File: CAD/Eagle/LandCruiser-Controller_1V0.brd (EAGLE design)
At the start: 99 x 67.7 mm, 21 parts, among them U101 MEGA8-P, X301 I2C

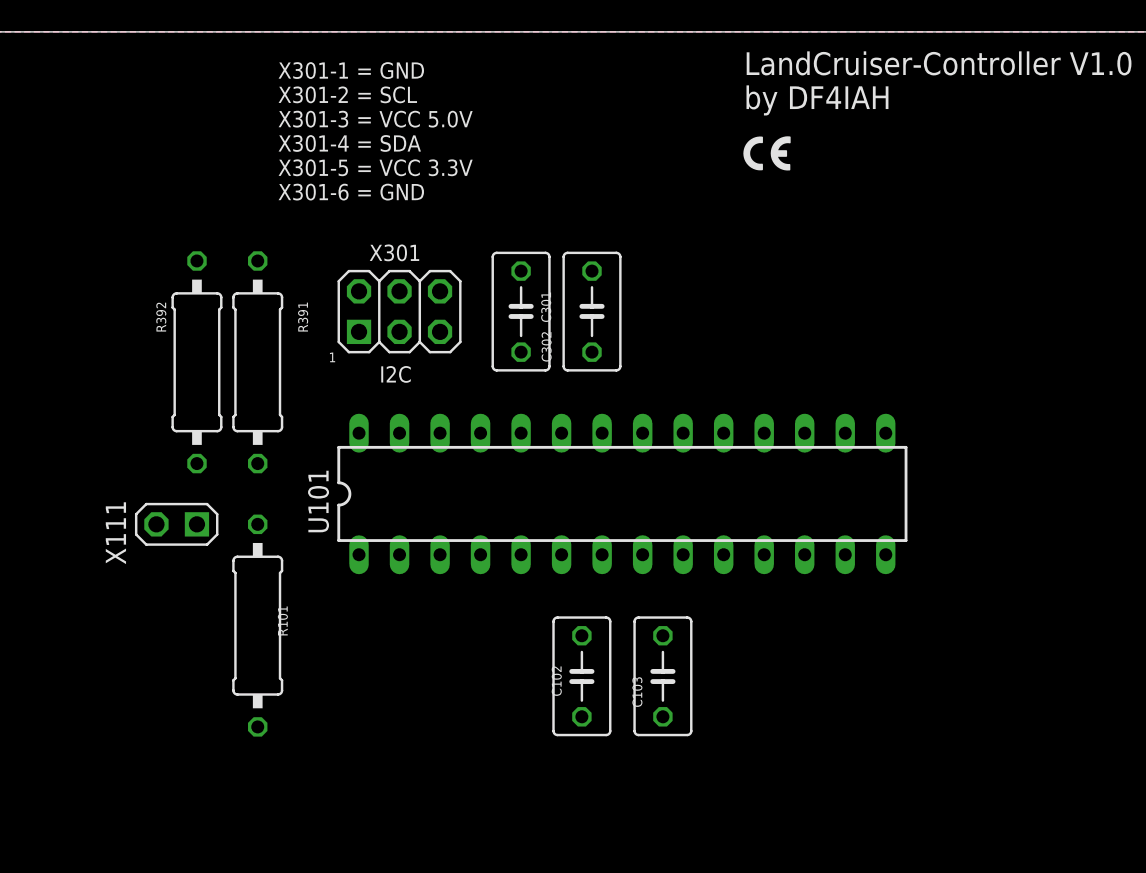
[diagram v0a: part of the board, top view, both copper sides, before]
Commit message: HW - pull-down resistors added to the ATmega output lines
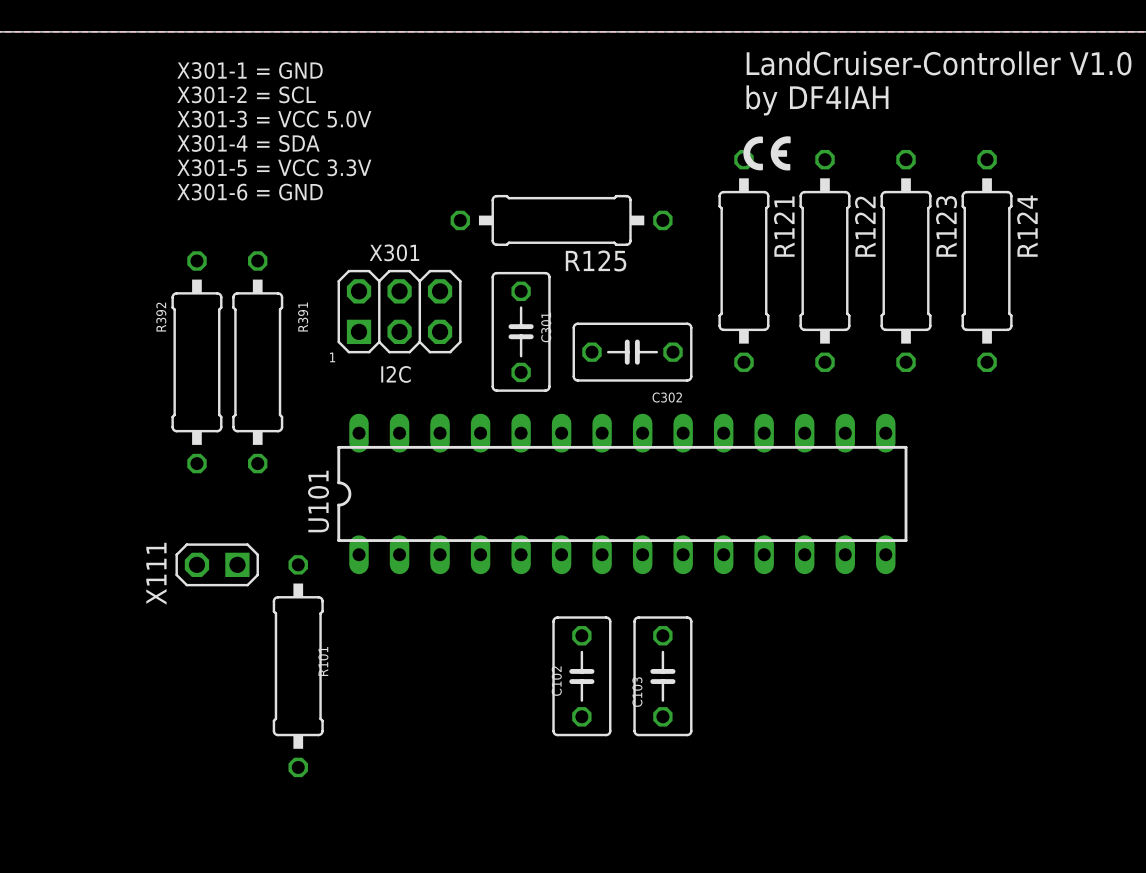
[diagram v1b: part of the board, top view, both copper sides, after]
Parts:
- added R121, R122, R123, R124, R125: 33kR, rcl:0309/12
- moved C302 3.59 mm to (50.2, 47.6), turned to 180 degrees
- moved R101 3.59 mm to (29.2, 27.9)
- moved X111 3.59 mm to (25.4, 34.3)
- moved C301 1.27 mm to (43.2, 48.9)
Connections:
- net GND: now also R121.1, R122.1, R123.1, R124.1, R125.1
- net MP_KL: now also R125.2
- net MP_M1: now also R123.2
- net MP_M2: now also R124.2
- net MP_PV_G: now also R121.2
- net MP_PV_O: now also R122.2
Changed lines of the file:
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@@
 <dimension x1="0" y1="0" x2="0" y2="7.5" x3="-3.5" y3="3.75" textsize="0.6096" layer="47"/>
 <text x="31.115" y="46.99" size="0.6096" layer="21" ratio="20">1</text>
-<text x="27.94" y="57.15" size="1.016" layer="21">X301-1 = GND
+<text x="21.59" y="57.15" size="1.016" layer="21">X301-1 = GND
 X301-2 = SCL
 X301-3 = VCC 5.0V
@@
 <attribute name="VALUE" x="23.495" y="45.72" size="0.6096" layer="27" rot="R90"/>
 </element>
-<element name="C302" library="rcl" package="C050-035X075" value="100nF" x="47.625" y="50.165" smashed="yes" rot="R90">
-<attribute name="NAME" x="45.085" y="46.99" size="0.6096" layer="25" rot="R90"/>
-<attribute name="VALUE" x="48.26" y="48.895" size="0.6096" layer="27" rot="R90"/>
-</element>
-<element name="C301" library="rcl" package="C050-035X075" value="100nF" x="43.18" y="50.165" smashed="yes" rot="R90">
-<attribute name="NAME" x="44.45" y="51.435" size="0.6096" layer="25" rot="R270"/>
-<attribute name="VALUE" x="42.545" y="51.435" size="0.6096" layer="27" rot="R270"/>
+<element name="C302" library="rcl" package="C050-035X075" value="100nF" x="50.165" y="47.625" smashed="yes" rot="R180">
+<attribute name="NAME" x="53.34" y="45.085" size="0.6096" layer="25" rot="R180"/>
+<attribute name="VALUE" x="51.435" y="48.26" size="0.6096" layer="27" rot="R180"/>
+</element>
+<element name="C301" library="rcl" package="C050-035X075" value="100nF" x="43.18" y="48.895" smashed="yes" rot="R90">
+<attribute name="NAME" x="44.45" y="50.165" size="0.6096" layer="25" rot="R270"/>
+<attribute name="VALUE" x="42.545" y="50.165" size="0.6096" layer="27" rot="R270"/>
 </element>
 <element name="C102" library="rcl" package="C050-035X075" value="100nF" x="46.99" y="27.305" smashed="yes" rot="R270">
@@
 <attribute name="VALUE" x="52.705" y="26.035" size="0.6096" layer="27" rot="R90"/>
 </element>
-<element name="R101" library="rcl" package="0309/12" value="12kR" x="26.67" y="30.48" smashed="yes" rot="R90">
-<attribute name="NAME" x="27.94" y="31.75" size="0.6096" layer="25" rot="R270"/>
-<attribute name="VALUE" x="26.035" y="31.115" size="0.6096" layer="27" rot="R270"/>
+<element name="R101" library="rcl" package="0309/12" value="12kR" x="29.21" y="27.94" smashed="yes" rot="R90">
+<attribute name="NAME" x="30.48" y="29.21" size="0.6096" layer="25" rot="R270"/>
+<attribute name="VALUE" x="28.575" y="28.575" size="0.6096" layer="27" rot="R270"/>
 </element>
 <element name="U101" library="df4iah_processors" package="DIL28-3" value="MEGA8-P" x="49.53" y="38.735"/>
@@
 <element name="FM503" library="df4iah_fiducial" package="FIDUCIAL_MARK_1MM" value="FIDUCIAL_MARK_1MM" x="95.25" y="54.61"/>
 <element name="FM504" library="df4iah_fiducial" package="FIDUCIAL_MARK_1MM" value="FIDUCIAL_MARK_1MM" x="95.25" y="11.43"/>
-<element name="X111" library="df4iah_connector" package="1X02" value="" x="22.86" y="36.83" rot="R90"/>
+<element name="X111" library="df4iah_connector" package="1X02" value="" x="25.4" y="34.29" rot="R90"/>
+<element name="R121" library="rcl" package="0309/12" value="33kR" x="57.15" y="53.34" rot="R270"/>
+<element name="R123" library="rcl" package="0309/12" value="33kR" x="67.31" y="53.34" rot="R270"/>
+<element name="R125" library="rcl" package="0309/12" value="33kR" x="45.72" y="55.88" rot="R180"/>
+<element name="R122" library="rcl" package="0309/12" value="33kR" x="62.23" y="53.34" rot="R270"/>
+<element name="R124" library="rcl" package="0309/12" value="33kR" x="72.39" y="53.34" rot="R270"/>
 </elements>
 <signals>
@@
 <vertex x="99.06" y="0"/>
 </polygon>
-<contactref element="C102" pad="2"/>
 <contactref element="C101" pad="2"/>
 <contactref element="U101" pad="8"/>
@@
 <contactref element="H504" pad="B2,8"/>
 <contactref element="X111" pad="2"/>
+<contactref element="R125" pad="1"/>
+<contactref element="R122" pad="1"/>
+<contactref element="R124" pad="1"/>
+<contactref element="R121" pad="1"/>
+<contactref element="R123" pad="1"/>
+<contactref element="C102" pad="2"/>
+<wire x1="72.39" y1="59.69" x2="93.77" y2="62.5" width="0" layer="19" extent="1-1"/>
+<wire x1="67.31" y1="59.69" x2="72.39" y2="59.69" width="0" layer="19" extent="1-1"/>
+<wire x1="62.23" y1="59.69" x2="67.31" y2="59.69" width="0" layer="19" extent="1-1"/>
+<wire x1="57.15" y1="59.69" x2="62.23" y2="59.69" width="0" layer="19" extent="1-1"/>
+<wire x1="52.07" y1="55.88" x2="57.15" y2="59.69" width="0" layer="19" extent="1-1"/>
+<wire x1="47.625" y1="47.625" x2="52.07" y2="55.88" width="0" layer="19" extent="1-1"/>
+<wire x1="48.26" y1="42.545" x2="47.625" y2="47.625" width="0" layer="19" extent="1-1"/>
+<wire x1="43.18" y1="51.435" x2="47.625" y2="47.625" width="0" layer="19" extent="1-1"/>
+<wire x1="38.1" y1="51.435" x2="43.18" y2="51.435" width="0" layer="19" extent="1-1"/>
+<wire x1="33.02" y1="48.895" x2="38.1" y2="51.435" width="0" layer="19" extent="1-1"/>
+<wire x1="50.8" y1="34.925" x2="48.26" y2="42.545" width="0" layer="19" extent="1-1"/>
+<wire x1="52.07" y1="29.845" x2="50.8" y2="34.925" width="0" layer="19" extent="1-1"/>
+<wire x1="46.99" y1="24.765" x2="52.07" y2="29.845" width="0" layer="19" extent="1-1"/>
+<wire x1="22.86" y1="34.29" x2="33.02" y2="48.895" width="0" layer="19" extent="1-1"/>
+<wire x1="4.96" y1="62.5" x2="33.02" y2="48.895" width="0" layer="19" extent="1-1"/>
 <wire x1="92.71" y1="29.972" x2="93.77" y2="62.5" width="0" layer="19" extent="1-1"/>
 <wire x1="93.77" y1="4.96" x2="92.71" y2="29.972" width="0" layer="19" extent="1-1"/>
-<wire x1="52.07" y1="29.845" x2="92.71" y2="29.972" width="0" layer="19" extent="1-1"/>
-<wire x1="50.8" y1="34.925" x2="52.07" y2="29.845" width="0" layer="19" extent="1-1"/>
-<wire x1="46.99" y1="24.765" x2="52.07" y2="29.845" width="0" layer="19" extent="1-1"/>
-<wire x1="48.26" y1="42.545" x2="50.8" y2="34.925" width="0" layer="19" extent="1-1"/>
-<wire x1="47.625" y1="52.705" x2="48.26" y2="42.545" width="0" layer="19" extent="1-1"/>
-<wire x1="43.18" y1="52.705" x2="47.625" y2="52.705" width="0" layer="19" extent="1-1"/>
-<wire x1="38.1" y1="51.435" x2="43.18" y2="52.705" width="0" layer="19" extent="1-1"/>
-<wire x1="33.02" y1="48.895" x2="38.1" y2="51.435" width="0" layer="19" extent="1-1"/>
-<wire x1="20.32" y1="36.83" x2="33.02" y2="48.895" width="0" layer="19" extent="1-1"/>
-<wire x1="4.96" y1="62.5" x2="20.32" y2="36.83" width="0" layer="19" extent="1-1"/>
-<wire x1="4.96" y1="4.96" x2="20.32" y2="36.83" width="0" layer="19" extent="1-1"/>
+<wire x1="4.96" y1="4.96" x2="22.86" y2="34.29" width="0" layer="19" extent="1-1"/>
 </signal>
 <signal name="+5V">
 <contactref element="X301" pad="3"/>
 <contactref element="C301" pad="1"/>
-<wire x1="35.56" y1="48.895" x2="43.18" y2="47.625" width="0" layer="19" extent="1-1"/>
+<wire x1="35.56" y1="48.895" x2="43.18" y2="46.355" width="0" layer="19" extent="1-1"/>
 </signal>
 <signal name="+3V3">
@@
 <contactref element="U101" pad="7"/>
 <wire x1="53.34" y1="42.545" x2="92.71" y2="44.958" width="0" layer="19" extent="1-1"/>
-<wire x1="47.625" y1="47.625" x2="53.34" y2="42.545" width="0" layer="19" extent="1-1"/>
+<wire x1="52.705" y1="47.625" x2="53.34" y2="42.545" width="0" layer="19" extent="1-1"/>
 <wire x1="48.26" y1="34.925" x2="53.34" y2="42.545" width="0" layer="19" extent="1-1"/>
 <wire x1="46.99" y1="29.845" x2="48.26" y2="34.925" width="0" layer="19" extent="1-1"/>
-<wire x1="38.1" y1="48.895" x2="47.625" y2="47.625" width="0" layer="19" extent="1-1"/>
+<wire x1="38.1" y1="48.895" x2="52.705" y2="47.625" width="0" layer="19" extent="1-1"/>
 <wire x1="26.67" y1="53.34" x2="38.1" y2="48.895" width="0" layer="19" extent="1-1"/>
 <wire x1="22.86" y1="53.34" x2="26.67" y2="53.34" width="0" layer="19" extent="1-1"/>
-<wire x1="26.67" y1="24.13" x2="46.99" y2="29.845" width="0" layer="19" extent="1-1"/>
+<wire x1="29.21" y1="21.59" x2="46.99" y2="29.845" width="0" layer="19" extent="1-1"/>
 </signal>
 <signal name="SCL">
@@
 <contactref element="R101" pad="2"/>
 <contactref element="X111" pad="1"/>
-<wire x1="26.67" y1="36.83" x2="33.02" y2="34.925" width="0" layer="19" extent="1-1"/>
-<wire x1="22.86" y1="36.83" x2="26.67" y2="36.83" width="0" layer="19" extent="1-1"/>
+<wire x1="29.21" y1="34.29" x2="33.02" y2="34.925" width="0" layer="19" extent="1-1"/>
+<wire x1="25.4" y1="34.29" x2="29.21" y2="34.29" width="0" layer="19" extent="1-1"/>
 </signal>
 <signal name="AREF">
@@
 <signal name="MP_M2">
 <contactref element="U101" pad="16"/>
+<contactref element="R124" pad="2"/>
+<wire x1="63.5" y1="42.545" x2="72.39" y2="46.99" width="0" layer="19" extent="1-1"/>
 </signal>
 <signal name="MP_M1">
 <contactref element="U101" pad="17"/>
+<contactref element="R123" pad="2"/>
+<wire x1="60.96" y1="42.545" x2="67.31" y2="46.99" width="0" layer="19" extent="1-1"/>
 </signal>
 <signal name="MP_PV_O">
 <contactref element="U101" pad="18"/>
+<contactref element="R122" pad="2"/>
+<wire x1="58.42" y1="42.545" x2="62.23" y2="46.99" width="0" layer="19" extent="1-1"/>
 </signal>
 <signal name="MP_PV_G">
 <contactref element="U101" pad="19"/>
+<contactref element="R121" pad="2"/>
+<wire x1="55.88" y1="42.545" x2="57.15" y2="46.99" width="0" layer="19" extent="1-1"/>
 </signal>
 <signal name="MP_KL">
 <contactref element="U101" pad="26"/>
+<contactref element="R125" pad="2"/>
+<wire x1="38.1" y1="42.545" x2="39.37" y2="55.88" width="0" layer="19" extent="1-1"/>
 </signal>
 </signals>

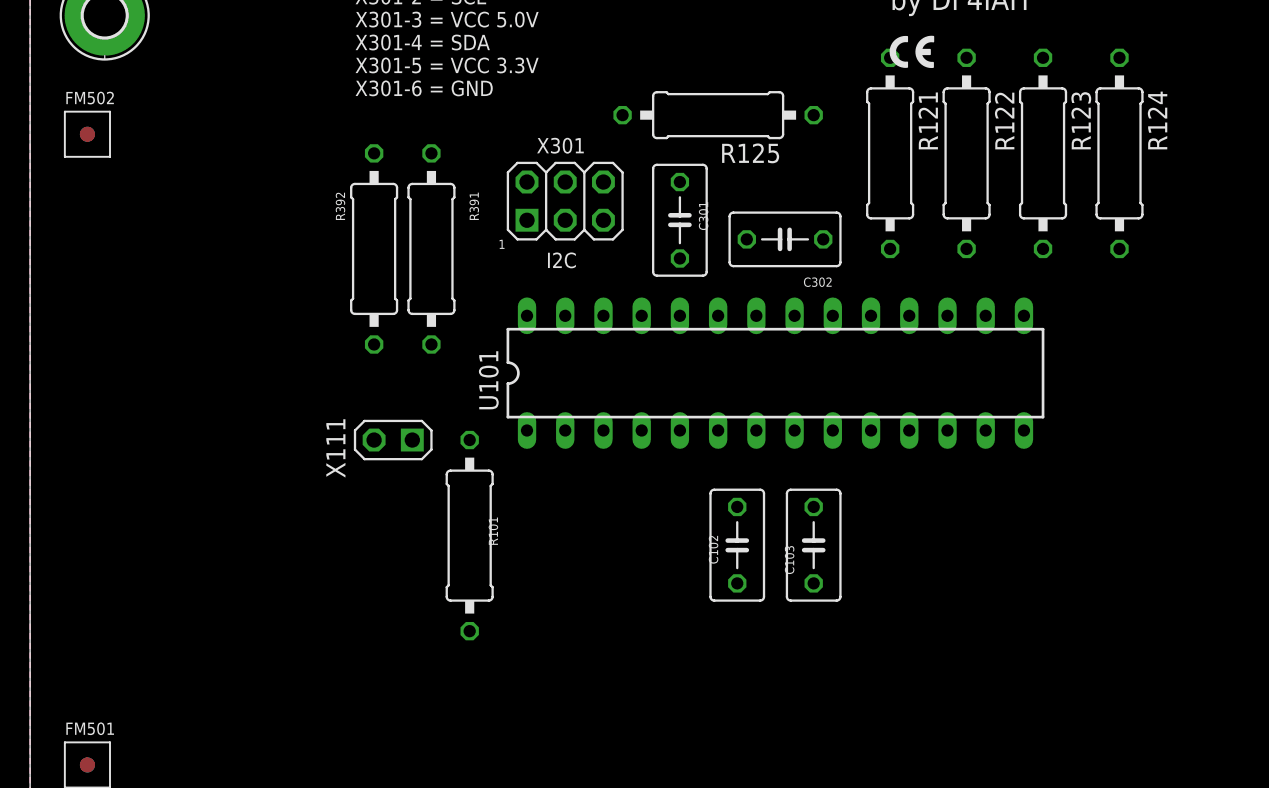
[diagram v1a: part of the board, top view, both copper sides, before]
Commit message: HW - pull-up resistors added to the ATmega input lines
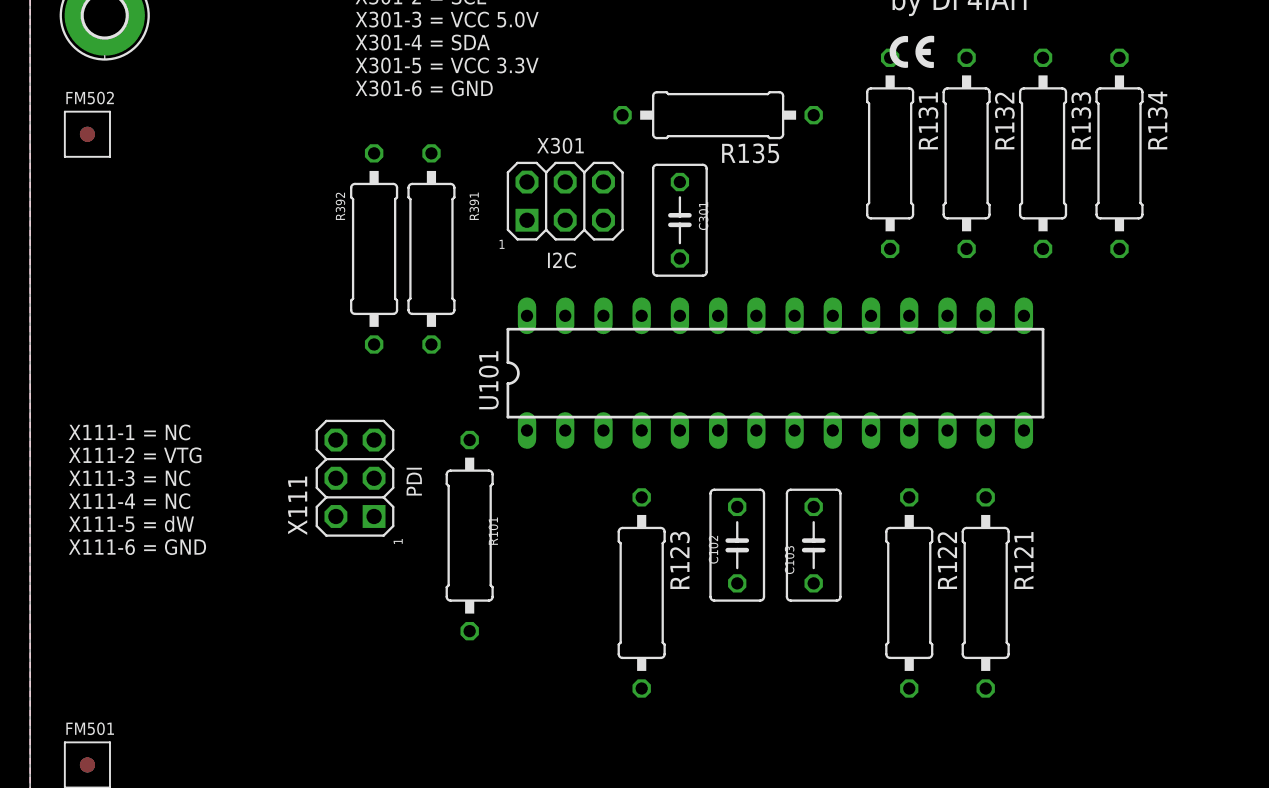
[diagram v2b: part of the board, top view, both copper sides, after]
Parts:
- removed C302: 100nF, rcl:C050-035X075
- added R131, R132, R133: 33kR, rcl:0309/12
- R121, R122, R123: value 33kR -> 4k7R
- R391, R392: value 1kR -> 2k2R
- X111: device df4iah_connector:1X02 -> df4iah_connector:2X03
- moved R123 39.6 mm to (40.6, 24.1)
- moved R121 29.9 mm to (63.5, 24.1)
- moved R122 29.5 mm to (58.4, 24.1)
- moved X111 4.58 mm to (21.6, 31.8)
- renumbered R124 to R134, R125 to R135
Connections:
- removed net +3V3: C101.1, C102.1, C302.1, R101.1, R391.2, R392.2, U101.20, U101.7, X301.5
- net !RST: now also X111.5; no longer X111.1
- net +5V: now also C101.1, C102.1, R101.1, R121.2, R122.2, R123.2, R391.2, R392.2, U101.20, U101.7, X111.2
- net GND: now also R131.1, R132.1, R133.1, X111.6; no longer C302.2, R121.1, R122.1, R123.1, X111.2
- net MP_FB: now also R123.1
- net MP_M1: now also R133.2; no longer R123.2
- net MP_PV_G: now also R131.2; no longer R121.2
- net MP_PV_O: now also R132.2; no longer R122.2
- net MP_SA_G: now also R122.1
- net MP_SA_O: now also R121.1
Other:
- board text added: "PDI"
- board text added: "X111-1 = NC X111-2 = VTG X111-3 = NC X111-4 = NC X111-5 = dW X111-6 = GND"
